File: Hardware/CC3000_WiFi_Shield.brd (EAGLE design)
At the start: 69.8 x 53.3 mm, 32 parts, among them J1 U.FL, U1 V_REG_317SMD, U2 ARDUINO_SHIELDLABEL, U3 74HC4050, U4 USD-SOCKETNEW, U5 CC3000

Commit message: Prototype board ready for review
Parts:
- C8: value 10pF -> DNP
- D1: value (none) -> GREEN
- JP1: value (none) -> Debug
- SJ1: value (none) -> Mode
- moved FRAME1 121.8 mm to (0.00, -16.5)
- moved LOGO3 48.9 mm to (31.8, 26.7)
- moved LOGO2 42.7 mm to (9.91, 21.8), flipped to the bottom, turned to 270 degrees
- moved LOGO1 24.5 mm to (5.08, 24.1)
- moved FID1 17.8 mm to (53.3, 5.08)
- moved L2 1.43 mm to (62.6, 20.5)
- moved AE1 1.27 mm to (63.5, 31.8), turned to 90 degrees
- moved C7 1.27 mm to (63.5, 22.9), turned to 270 degrees
- moved R4 1.27 mm to (47.0, 43.2), turned to 90 degrees
- moved L1 1.05 mm to (62.6, 25.1)
- turned R5 to 90 degrees
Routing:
- net N$5: track 0.00 -> 9.51 mm
- net 3.3V: track 134.8 -> 143.2 mm
- net N$9: track 0.00 -> 7.12 mm
- net N$8: track 0.00 -> 4.19 mm
- net N$10: track 0.00 -> 4.05 mm
- net SD_CS: track 90.3 -> 86.8 mm
- net WIFI_CS: track 65.7 -> 62.7 mm
- net SPI_SCK: track 85.1 -> 86.4 mm
- net WIFI_EN: track 78.9 -> 77.8 mm
- net D13: track 43.3 -> 42.3 mm
- net D2: track 25.1 -> 26.0 mm
- net D11: track 35.1 -> 34.5 mm
- net D4: track 25.3 -> 24.7 mm
- added copper zone on layer 16, net GND
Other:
- board text added: "802.11b/g"
- board text added: "CC3000"
- board text added: "Debug"
- board text added: "GND"
- board text added: "MISO/"
- board text added: "MOSI/"
- board text added: "PWR"
- board text added: "RF_CS/"
- board text added: "RF_EN/"
- board text added: "RF_INT/"
- board text added: "RX"
- board text added: "Reset"
- board text added: "SCK/"
- board text added: "SD_CS/"
- board text added: "Shawn Hymel"
- board text added: "TX"
- board text added: "WiFi Shield"
- board text added: "v01"

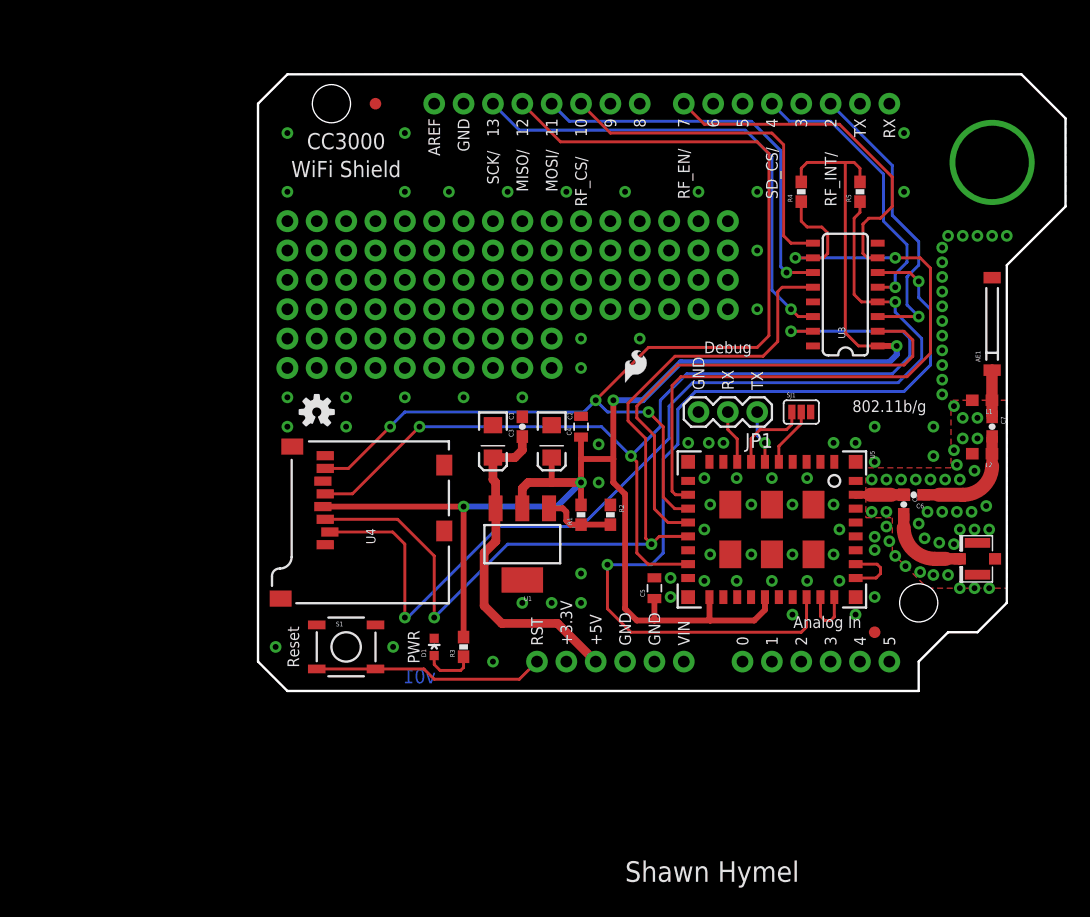
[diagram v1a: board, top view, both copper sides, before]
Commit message: Fixed floating 3.3V paddle on LM317. Made stitching vias near RF section 10 mils.
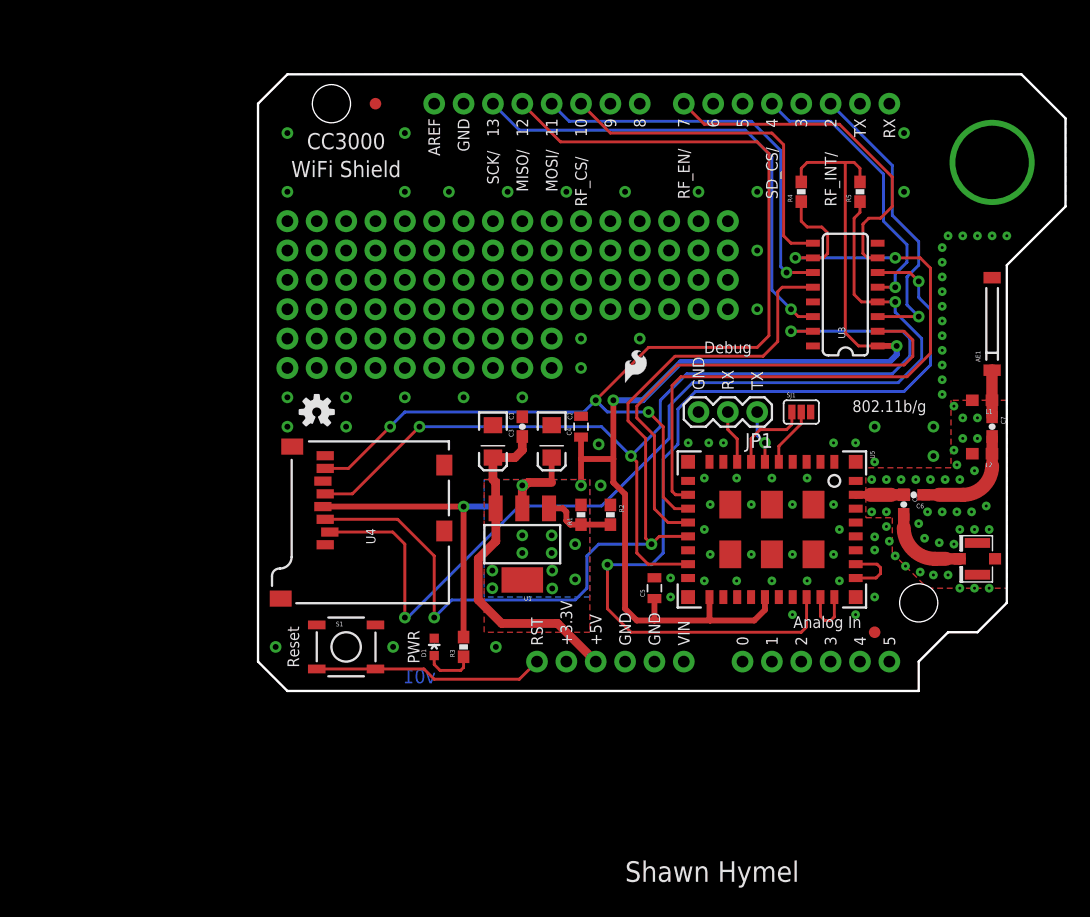
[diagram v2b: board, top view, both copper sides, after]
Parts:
- U1: value V_REG_317SMD -> (none)
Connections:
- net 3.3V: now also U1.4
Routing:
- net 3.3V: track 143.2 -> 131.0 mm, vias 4 -> 15
- net SPI_MOSI: track 76.7 -> 78.3 mm
- added copper zone on layer 1, net 3.3V
- added copper zone on layer 16, net 3.3V
